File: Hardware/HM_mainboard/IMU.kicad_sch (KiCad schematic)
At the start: 3 parts

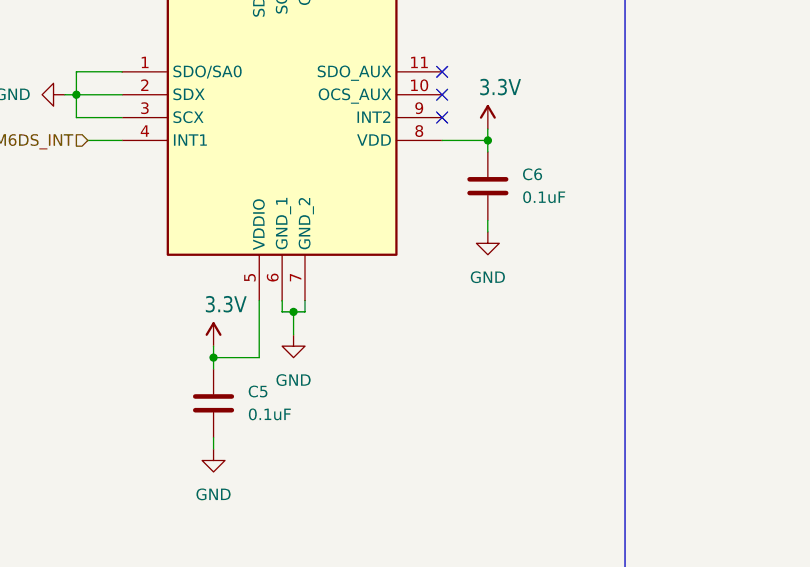
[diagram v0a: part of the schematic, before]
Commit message: Updated port connectors of microcontroller
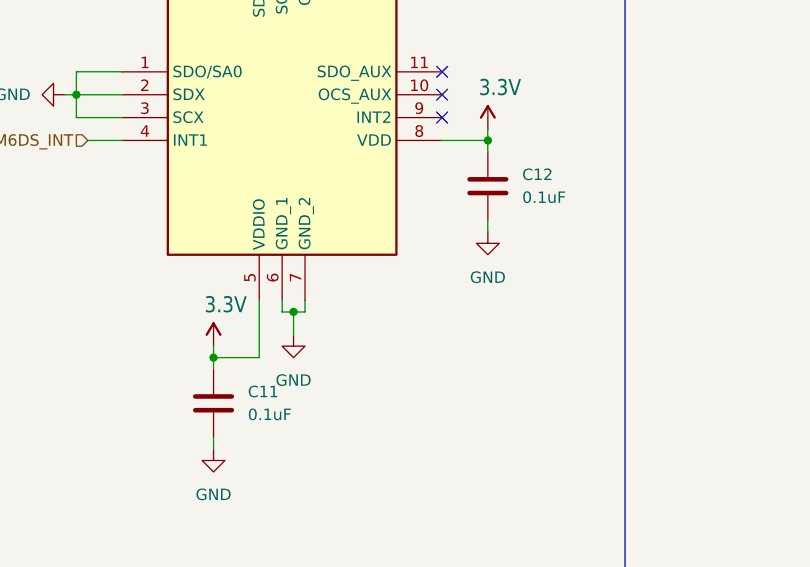
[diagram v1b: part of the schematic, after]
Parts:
- renumbered C5 to C11, C6 to C12
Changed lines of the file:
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@@
         )
         (path "/54a6df43-5475-46a2-9916-8b0260700d4c/9043a365-e24a-41b8-9f6d-decb4da0da6a"
-          (reference "#PWR010") (unit 1)
+          (reference "#PWR029") (unit 1)
         )
       )
@@
         )
         (path "/54a6df43-5475-46a2-9916-8b0260700d4c/9043a365-e24a-41b8-9f6d-decb4da0da6a"
-          (reference "#SUPPLY013") (unit 1)
+          (reference "#SUPPLY017") (unit 1)
         )
       )
@@
         )
         (path "/54a6df43-5475-46a2-9916-8b0260700d4c/9043a365-e24a-41b8-9f6d-decb4da0da6a"
-          (reference "#SUPPLY012") (unit 1)
+          (reference "#SUPPLY016") (unit 1)
         )
       )
@@
         )
         (path "/54a6df43-5475-46a2-9916-8b0260700d4c/9043a365-e24a-41b8-9f6d-decb4da0da6a"
-          (reference "#PWR09") (unit 1)
+          (reference "#PWR028") (unit 1)
         )
       )
@@
   (symbol (lib_id "Device:C") (at 95.25 113.03 0) (unit 1)
     (in_bom yes) (on_board yes) (dnp no) (fields_autoplaced)
-    (property "Reference" "C5" (at 99.06 111.76 0)
+    (property "Reference" "C11" (at 99.06 111.76 0)
       (effects (font (size 1.27 1.27)) (justify left))
     )
@@
       (project "HM_mainboard"
         (path "/54a6df43-5475-46a2-9916-8b0260700d4c/9043a365-e24a-41b8-9f6d-decb4da0da6a"
-          (reference "C5") (unit 1)
+          (reference "C11") (unit 1)
         )
       )
@@
   (symbol (lib_id "Device:C") (at 125.73 88.9 0) (unit 1)
     (in_bom yes) (on_board yes) (dnp no) (fields_autoplaced)
-    (property "Reference" "C6" (at 129.54 87.63 0)
+    (property "Reference" "C12" (at 129.54 87.63 0)
       (effects (font (size 1.27 1.27)) (justify left))
     )
@@
       (project "HM_mainboard"
         (path "/54a6df43-5475-46a2-9916-8b0260700d4c/9043a365-e24a-41b8-9f6d-decb4da0da6a"
-          (reference "C6") (unit 1)
+          (reference "C12") (unit 1)
         )
       )
@@
         )
         (path "/54a6df43-5475-46a2-9916-8b0260700d4c/9043a365-e24a-41b8-9f6d-decb4da0da6a"
-          (reference "#SUPPLY014") (unit 1)
+          (reference "#SUPPLY018") (unit 1)
         )
       )
@@
         )
         (path "/54a6df43-5475-46a2-9916-8b0260700d4c/9043a365-e24a-41b8-9f6d-decb4da0da6a"
-          (reference "#PWR011") (unit 1)
+          (reference "#PWR030") (unit 1)
         )
       )
@@
         )
         (path "/54a6df43-5475-46a2-9916-8b0260700d4c/9043a365-e24a-41b8-9f6d-decb4da0da6a"
-          (reference "#PWR012") (unit 1)
-        )
-      )
+          (reference "#PWR031") (unit 1)
+        )
+      )

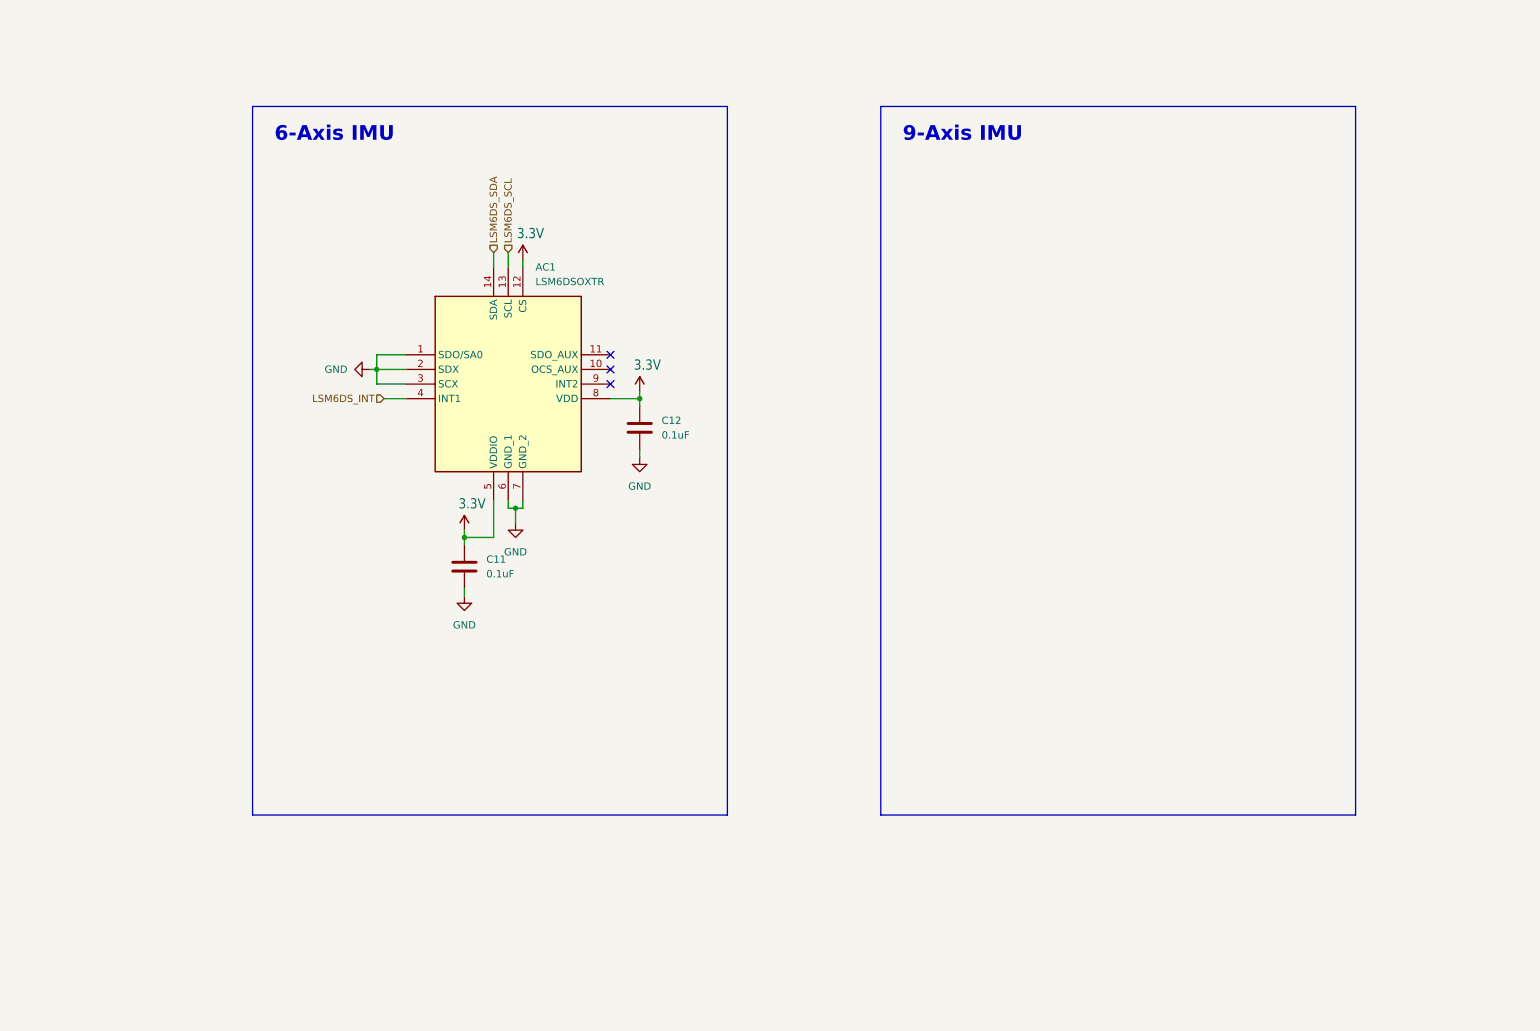
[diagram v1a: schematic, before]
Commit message: Added IMUs, updated some components
- Added 2 additonal IMUs:
     1) 6-Axis MC6470
     2) 9-Axis BNO55
- Replaced button jack connectors
- Replaced battery charging LED by a charging status measurement circuit
- Replaced caps for clock crystal
- Added stabalizing caps to uC Vcc
- Added UART pin header
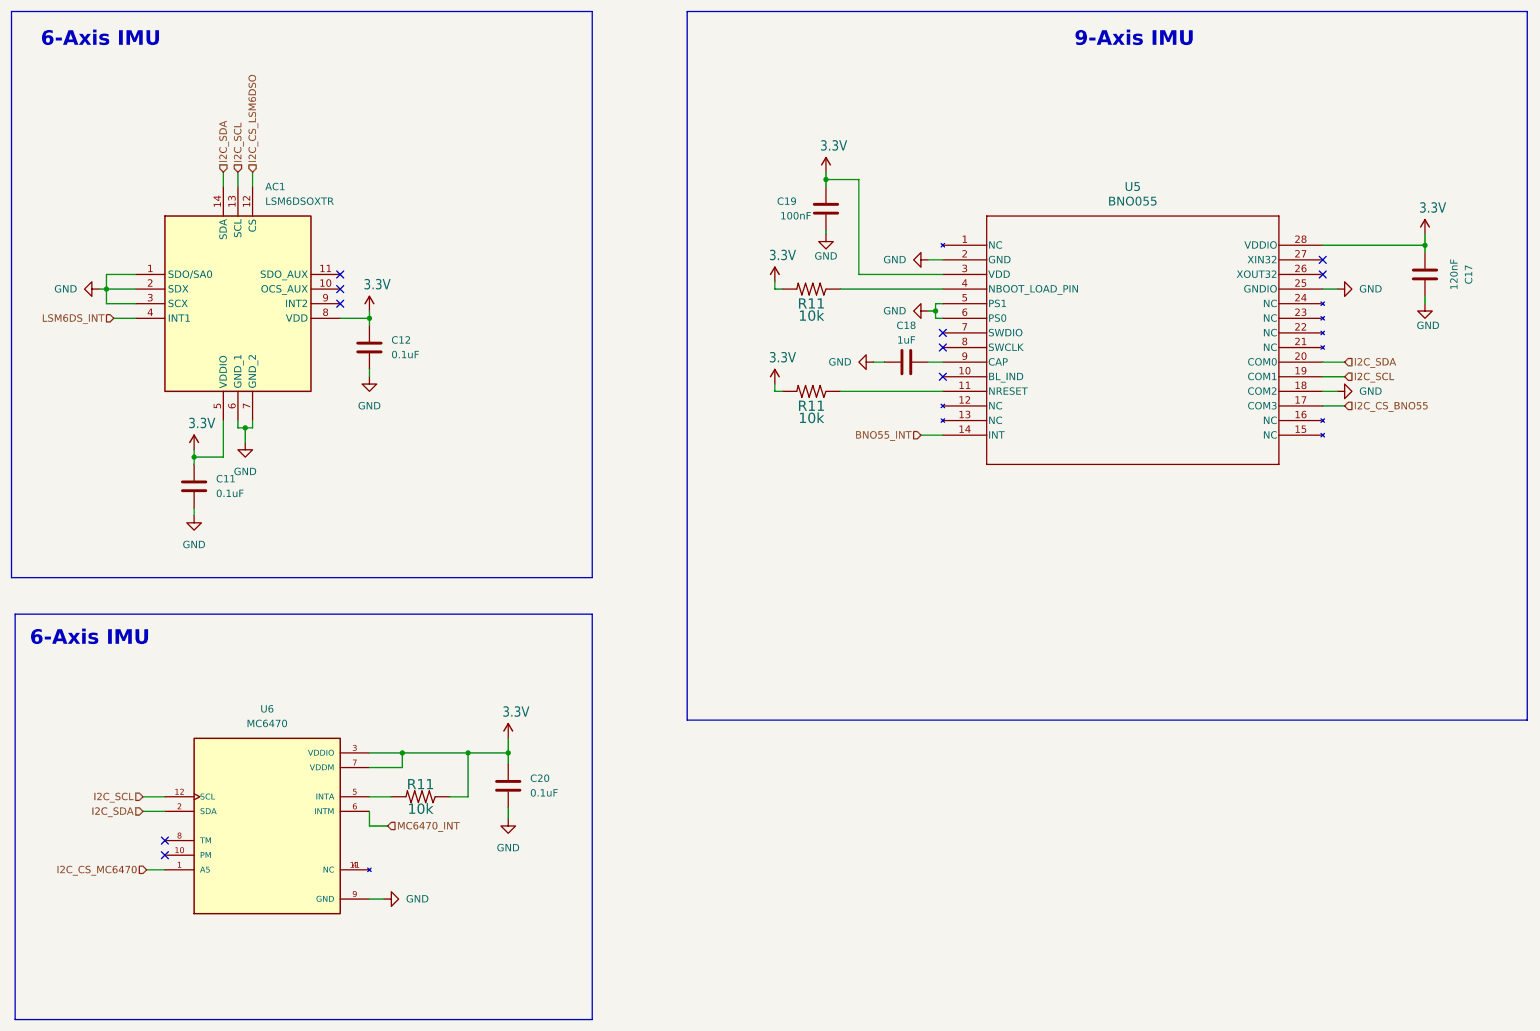
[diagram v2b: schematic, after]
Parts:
- added C17: 120nF, Capacitor_SMD:C_0603_1608Metric_Pad1.08x0.95mm_HandSolder, symbol Device:C
- added C18: 1uF, Capacitor_SMD:C_0603_1608Metric_Pad1.08x0.95mm_HandSolder, symbol Device:C
- added C19: 100nF, Capacitor_SMD:C_0603_1608Metric_Pad1.08x0.95mm_HandSolder, symbol Device:C
- added C20: 0.1uF, Capacitor_SMD:C_0603_1608Metric_Pad1.08x0.95mm_HandSolder, symbol Device:C
- added R11 (x3): 10k, Resistor_SMD:R_0603_1608Metric_Pad0.98x0.95mm_HandSolder, symbol esp32-thing-eagle-import:10KOHM-1/10W-1%(0603)0603
- added U5: BNO055, HeadMouse:QFN_BNO055_BOS, symbol HeadMouse:BNO055
- added U6: MC6470, HeadMouse:PQFN50P200X200X100-12N, symbol HeadMouse:MC6470
- C11, C12: footprint Capacitor_SMD:C_0201_0603Metric_Pad0.64x0.40mm_HandSolder -> Capacitor_SMD:C_0603_1608Metric_Pad1.08x0.95mm_HandSolder
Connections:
- net 3.3V: now also C17.1, C19.1, C20.1, R11.1, R11.2, R11.2, U5.28 (VDDIO), U5.3 (VDD), U6.3 (VDDIO), U6.7 (VDDM); no longer AC1.12 (CS)
- net GND: now also C17.2, C18.1, C19.2, C20.2, U5.18 (COM2), U5.2 (GND), U5.25 (GNDIO), U5.5 (PS1), U5.6 (PS0), U6.9 (GND)
- net LSM6DS_SCL renamed I2C_SCL
- net I2C_SCL: now also U5.19 (COM1), U6.12 (SCL)
- net LSM6DS_SDA renamed I2C_SDA
- net I2C_SDA: now also U5.20 (COM0), U6.2 (SDA)
- new net: C18.2, U5.9 (CAP)
- new net: R11.1, U5.4 (NBOOT_LOAD_PIN)
- new net: U6.11 (NC), U6.4 (NC)
- new net: R11.2, U6.5 (INTA)
- new net: R11.1, U5.11 (NRESET)
- new net BNO55_INT: U5.14 (INT)
- new net I2C_CS_BNO55: U5.17 (COM3)
- new net I2C_CS_LSM6DSO: AC1.12 (CS)
- new net I2C_CS_MC6470: U6.1 (A5)
- new net MC6470_INT: U6.6 (INTM)
- no-connect marks 3 -> 10
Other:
- moved on the sheet: AC1, C11, C12

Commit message: Changed I2C address selection of IMUs
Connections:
- net I2C_CS_BNO55 is gone; now on net GND: U5.17 (COM3)
- net I2C_CS_LSM6DSO is gone; now on net 3.3V: AC1.12 (CS)
- net I2C_CS_MC6470 is gone; now on net GND: U6.1 (A5)
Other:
- note added: "I2C slave addr.: 0b1001100 = 0x4c = 0d76"
- note added: "I2C slave addr.: 0b101000 = 0x28 = 0d40"
- note added: "I2C slave addr.: 0b1101010 = 0x6a = 0d106"
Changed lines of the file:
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@@
     (fill (type none))
   )
-  (text "9-Axis IMU" (at 201.295 22.86 0)
+  (text "9-Axis IMU" (at 140.97 24.13 0)
     (effects (font (size 2.54 2.54) (thickness 0.508) bold) (justify left bottom))
+  )
+  (text "I2C slave addr.: 0b1101010 = 0x6a = 0d106" (at 21.59 27.94 0)
+    (effects (font (size 1.27 1.27)) (justify left bottom))
+  )
+  (text "I2C slave addr.: 0b1001100 = 0x4c = 0d76" (at 20.32 132.715 0)
+    (effects (font (size 1.27 1.27)) (justify left bottom))
+  )
+  (text "I2C slave addr.: 0b101000 = 0x28 = 0d40" (at 141.605 30.48 0)
+    (effects (font (size 1.27 1.27)) (justify left bottom))
   )
   (text "6-Axis IMU" (at 21.59 22.86 0)
@@
     (effects (font (size 1.27 1.27)) (justify left))
   )
-  (hierarchical_label "I2C_CS_LSM6DSO" (shape input) (at 58.42 44.45 90) (fields_autoplaced)
-    (effects (font (size 1.27 1.27)) (justify left))
-  )
   (hierarchical_label "I2C_SDA" (shape input) (at 53.34 44.45 90) (fields_autoplaced)
     (effects (font (size 1.27 1.27)) (justify left))
@@
   )
   (hierarchical_label "I2C_SDA" (shape input) (at 248.285 77.47 0) (fields_autoplaced)
-    (effects (font (size 1.27 1.27)) (justify left))
-  )
-  (hierarchical_label "I2C_CS_MC6470" (shape input) (at 40.005 165.735 180) (fields_autoplaced)
-    (effects (font (size 1.27 1.27)) (justify right))
-  )
-  (hierarchical_label "I2C_CS_BNO55" (shape input) (at 248.285 85.09 0) (fields_autoplaced)
     (effects (font (size 1.27 1.27)) (justify left))
   )
@@
         (path "/54a6df43-5475-46a2-9916-8b0260700d4c/9043a365-e24a-41b8-9f6d-decb4da0da6a"
           (reference "#PWR042") (unit 1)
+        )
+      )
+    )
+  )
+  (symbol (lib_id "esp32-thing-eagle-import:3.3V") (at 58.42 44.45 0) (unit 1)
+    (in_bom yes) (on_board yes) (dnp no)
+    (property "Reference" "#SUPPLY08" (at 58.42 44.45 0)
+      (effects (font (size 1.27 1.27)) hide)
+    )
+    (property "Value" "3.3V" (at 57.404 40.894 0)
+      (effects (font (size 1.778 1.5113)) (justify left bottom))
+    )
+    (property "Footprint" "" (at 58.42 44.45 0)
+      (effects (font (size 1.27 1.27)) hide)
+    )
+    (property "Datasheet" "" (at 58.42 44.45 0)
+      (effects (font (size 1.27 1.27)) hide)
+    )
+    (pin "1")
+    (instances
+      (project "HM_mainboard"
+        (path "/54a6df43-5475-46a2-9916-8b0260700d4c"
+          (reference "#SUPPLY08") (unit 1)
+        )
+        (path "/54a6df43-5475-46a2-9916-8b0260700d4c/8a725ce3-408a-4762-9df2-b56094186e56"
+          (reference "#SUPPLY09") (unit 1)
+        )
+        (path "/54a6df43-5475-46a2-9916-8b0260700d4c/9043a365-e24a-41b8-9f6d-decb4da0da6a"
+          (reference "#SUPPLY024") (unit 1)
+        )
+      )
+      (project "esp32-thing"
+        (path "/64c5aff3-bdec-4fb6-b5ec-87e5efa2adf7"
+          (reference "#SUPPLY8") (unit 1)
         )
       )
@@
     )
   )
+  (symbol (lib_name "GND_1") (lib_id "power:GND") (at 248.285 85.09 90) (unit 1)
+    (in_bom yes) (on_board yes) (dnp no) (fields_autoplaced)
+    (property "Reference" "#PWR06" (at 254.635 85.09 0)
+      (effects (font (size 1.27 1.27)) hide)
+    )
+    (property "Value" "GND" (at 252.095 85.09 90)
+      (effects (font (size 1.27 1.27)) (justify right))
+    )
+    (property "Footprint" "" (at 248.285 85.09 0)
+      (effects (font (size 1.27 1.27)) hide)
+    )
+    (property "Datasheet" "" (at 248.285 85.09 0)
+      (effects (font (size 1.27 1.27)) hide)
+    )
+    (pin "1")
+    (instances
+      (project "HM_mainboard"
+        (path "/54a6df43-5475-46a2-9916-8b0260700d4c"
+          (reference "#PWR06") (unit 1)
+        )
+        (path "/54a6df43-5475-46a2-9916-8b0260700d4c/8a725ce3-408a-4762-9df2-b56094186e56"
+          (reference "#PWR09") (unit 1)
+        )
+        (path "/54a6df43-5475-46a2-9916-8b0260700d4c/9043a365-e24a-41b8-9f6d-decb4da0da6a"
+          (reference "#PWR048") (unit 1)
+        )
+      )
+    )
+  )
   (symbol (lib_id "Device:C") (at 158.115 50.8 0) (unit 1)
     (in_bom yes) (on_board yes) (dnp no)
@@
         )
       )
+    )
+  )
+  (symbol (lib_name "GND_1") (lib_id "power:GND") (at 40.005 165.735 270) (unit 1)
+    (in_bom yes) (on_board yes) (dnp no) (fields_autoplaced)
+    (property "Reference" "#PWR06" (at 33.655 165.735 0)
+      (effects (font (size 1.27 1.27)) hide)
+    )
+    (property "Value" "GND" (at 36.83 165.735 90)
+      (effects (font (size 1.27 1.27)) (justify right))
+    )
+    (property "Footprint" "" (at 40.005 165.735 0)
+      (effects (font (size 1.27 1.27)) hide)
+    )
+    (property "Datasheet" "" (at 40.005 165.735 0)
+      (effects (font (size 1.27 1.27)) hide)
+    )
+    (pin "1")
+    (instances
+      (project "HM_mainboard"
+        (path "/54a6df43-5475-46a2-9916-8b0260700d4c"
+          (reference "#PWR06") (unit 1)
+        )
+        (path "/54a6df43-5475-46a2-9916-8b0260700d4c/8a725ce3-408a-4762-9df2-b56094186e56"
+          (reference "#PWR09") (unit 1)
+        )
+        (path "/54a6df43-5475-46a2-9916-8b0260700d4c/9043a365-e24a-41b8-9f6d-decb4da0da6a"
+          (reference "#PWR049") (unit 1)
+        )
+      )
